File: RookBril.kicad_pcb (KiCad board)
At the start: 2 copper layers, 65 x 55 mm, 69 parts, among them J1 BATT_PINS, J10 TIM3_OUT_CONN, J12 Conn_01x04_Pin, J13 3V_MODE_PINS, J2 IR_SENSOR0_PINS, J3 IR_SENSOR1_PINS, J4 IR_SENSOR2_PINS, J5 IR_SENSOR3_PINS, J6 LOW-BAT_LED_CONN, J7 PDLC_JST_PINS, J9 MCU_MODE_PINS, SW1 SW_Push, U1 VNH7070ASTR, U2 TPS61170DRVR, U3 STM32F411RETx, U4 TPS631000DRLR, Y1 ABM3-8.000MHZ-D2Y-T

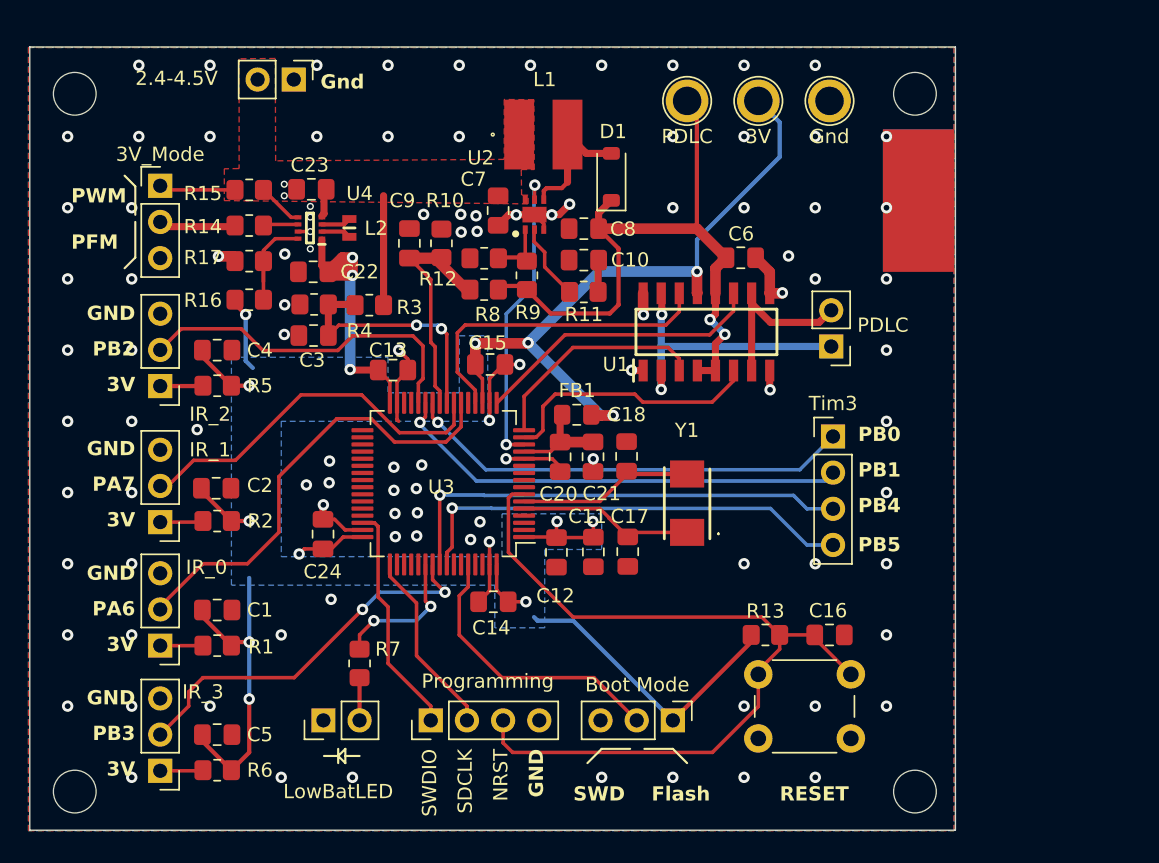
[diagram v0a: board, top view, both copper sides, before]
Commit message: PCBv2.01
Eerste versie van de tweede versie van de pcb prototype.
Nieuwe PDLC voeding, extra pinnen beschikbaar voor GUI inclusief voeding pinnen.
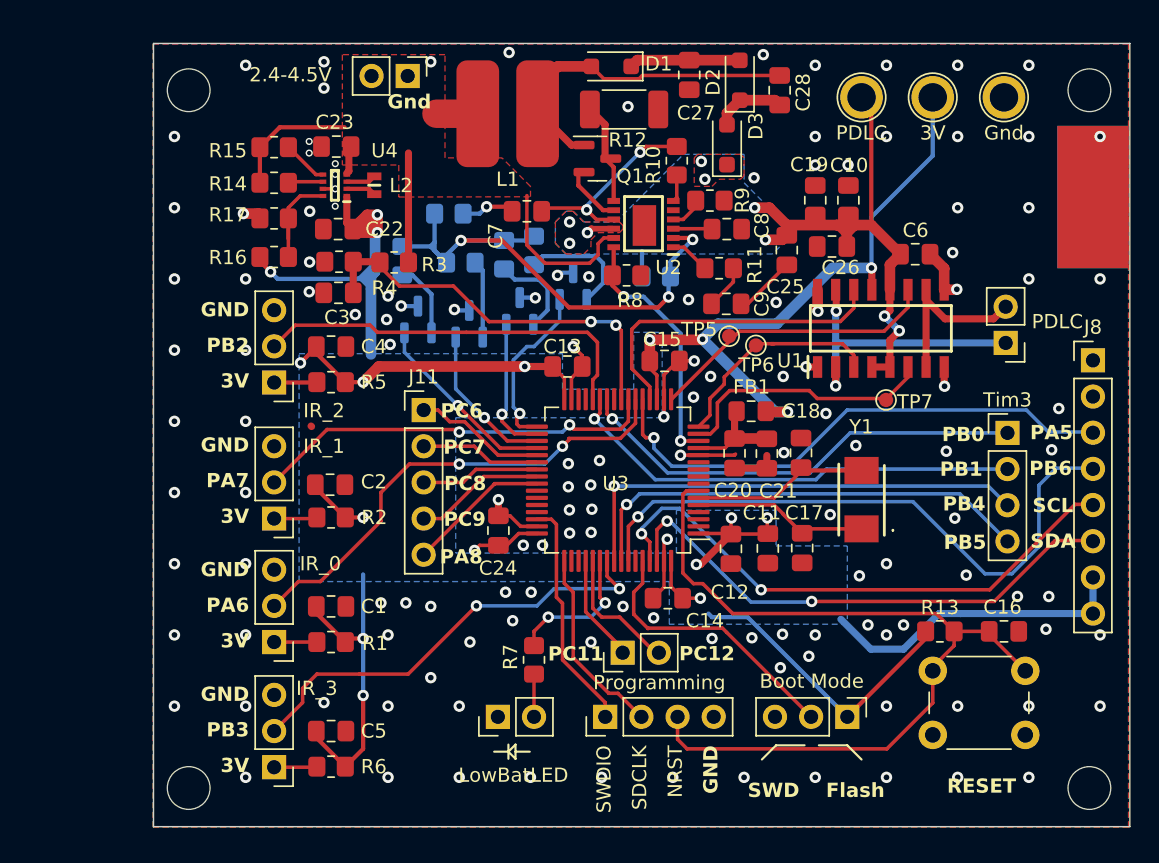
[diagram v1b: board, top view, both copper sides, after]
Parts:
- added C19: 10u, Capacitor_SMD:C_0805_2012Metric_Pad1.18x1.45mm_HandSolder, F.Cu at (170.0, 79.5)
- added C25: 10u, Capacitor_SMD:C_0805_2012Metric_Pad1.18x1.45mm_HandSolder, F.Cu at (168.0, 83.0)
- added C26: 10u, Capacitor_SMD:C_0805_2012Metric_Pad1.18x1.45mm_HandSolder, F.Cu at (171.2, 82.7)
- added C27: 10u, Capacitor_SMD:C_0805_2012Metric_Pad1.18x1.45mm_HandSolder, F.Cu at (161.2, 70.7)
- added C28: 100n, Capacitor_SMD:C_0805_2012Metric_Pad1.18x1.45mm_HandSolder, F.Cu at (167.5, 71.8)
- added D2: ~, Diode_SMD:D_SOD-123F, F.Cu at (164.7, 71.0)
- added D3: ~, Diode_SMD:D_SOD-123F, F.Cu at (163.8, 75.6)
- added J11: Conn_01x05_Pin, Connector_PinHeader_2.54mm:PinHeader_1x05_P2.54mm_Vertical, F.Cu at (142.5, 94.2)
- added J8: Conn_01x08_Pin, Connector_PinHeader_2.54mm:PinHeader_1x08_P2.54mm_Vertical, F.Cu at (189.5, 90.7)
- added Q1: NMOS, Package_TO_SOT_SMD:SOT-23, F.Cu at (154.7, 76.5)
- added Q2: NMOS, Package_TO_SOT_SMD:SOT-23, B.Cu at (142.1, 87.8)
- added Q3: NMOS, Package_TO_SOT_SMD:SOT-23, B.Cu at (145.7, 88.2)
- added Q4: NMOS, Package_TO_SOT_SMD:SOT-23, B.Cu at (149.2, 87.2)
- added Q5: NMOS, Package_TO_SOT_SMD:SOT-23, B.Cu at (153.0, 85.5)
- added R18: 590k, Resistor_SMD:R_0805_2012Metric_Pad1.20x1.40mm_HandSolder, B.Cu at (158.8, 84.8)
- added R19: 47.6k, Resistor_SMD:R_0805_2012Metric_Pad1.20x1.40mm_HandSolder, B.Cu at (144.3, 80.4)
- added R20: 160k, Resistor_SMD:R_0805_2012Metric_Pad1.20x1.40mm_HandSolder, B.Cu at (141.0, 83.7)
- added R21: 80k, Resistor_SMD:R_0805_2012Metric_Pad1.20x1.40mm_HandSolder, B.Cu at (145.1, 83.9)
- added R22: 40k, Resistor_SMD:R_0805_2012Metric_Pad1.20x1.40mm_HandSolder, B.Cu at (148.2, 83.3)
- added R23: 20k, Resistor_SMD:R_0805_2012Metric_Pad1.20x1.40mm_HandSolder, B.Cu at (150.2, 83.0)
- added TP5: TestPoint, TestPoint:TestPoint_Pad_D1.0mm, F.Cu at (163.9, 89.0)
- added TP6: TestPoint, TestPoint:TestPoint_Pad_D1.0mm, F.Cu at (165.8, 89.7)
- added TP7: TestPoint, TestPoint:TestPoint_Pad_D1.0mm, F.Cu at (175.0, 93.5)
- C10: value 680p -> 10u
- C7: value 10u -> 4.7u
- C8: value 10u -> 50n
- C9: value 100n -> 22n
- D1: value MBR0540 -> ~; footprint Diode_SMD:D_SOD-123 -> Diode_SMD:D_SOD-123F
- J13: value 3V_MODE_PINS -> GPIO_OUT_CONN; footprint Connector_PinHeader_2.54mm:PinHeader_1x03_P2.54mm_Vertical -> Connector_PinHeader_2.54mm:PinHeader_1x02_P2.54mm_Vertical
- L1: value VLCF5020T-100M1R1-1 -> 10u; footprint Components:VLCF5020 -> Components:MRS8030T100
- R10: value 10k -> 100k
- R11: value 10k -> 7.5k
- R12: value 39k -> 5m; footprint Resistor_SMD:R_0805_2012Metric_Pad1.20x1.40mm_HandSolder -> Resistor_SMD:R_2010_5025Metric_Pad1.40x2.65mm_HandSolder
- R3: value 50K -> 51k
- R8: value 62k -> 118k
- R9: value 10k -> 41.2k
- U2: value TPS61170DRVR -> ~; footprint Components:SON65P200X200X80-7N -> Components:LT3759
- moved J13 46.1 mm to (156.5, 111.2), turned to 90 degrees
- moved C9 22.7 mm to (163.8, 86.8), turned to 180 degrees
- moved C10 19.0 mm to (172.3, 79.5), turned to -90 degrees
- moved R10 17.5 mm to (160.3, 76.7)
- moved R12 14.3 mm to (156.6, 73.1)
- moved U2 14.0 mm to (163.8, 83.9), turned to 180 degrees
- moved R9 13.9 mm to (162.6, 79.5), turned to 0 degrees
- moved C24 12.3 mm to (147.8, 102.7)
- moved C11 12.3 mm to (166.7, 103.9)
- moved C12 12.3 mm to (164.1, 104.0)
- moved C13 12.3 mm to (152.6, 91.2)
- moved C14 12.3 mm to (159.6, 107.4)
- moved C15 12.3 mm to (159.4, 90.8)
- moved C16 12.3 mm to (183.2, 109.8)
- moved C17 12.3 mm to (169.1, 103.9)
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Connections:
- C10 pad 1: Net-(C10-Pad1) -> GND
- C10 pad 2: GND -> VCC
- C7 pad 1: +BATT -> GND
- C7 pad 2: GND -> Net-(U2-INTVcc)
- C8 pad 1: VCC -> GND
- C8 pad 2: GND -> Net-(U2-SS)
- C9 pad 1: /PDLC-BOOST_VOUT-FB -> GND
- C9 pad 2: GND -> Net-(C9-Pad2)
- D1 pad 1: VCC -> Net-(D1-K)
- J13 pad 1: +BATT -> /MCU/PC11
- J13 pad 2: Net-(J13-Pin_2) -> /MCU/PC12
- R10 pad 1: GND -> Net-(U2-INTVcc)
- R10 pad 2: /PDLC-BOOST_VOUT-FB -> Net-(U2-PGOOD)
- R11 pad 1: Net-(U2-COMP) -> Net-(C9-Pad2)
- R11 pad 2: Net-(C10-Pad1) -> Net-(U2-EN/UVLO)
- R12 pad 1: Net-(U2-FB) -> GND
- R12 pad 2: GND -> Net-(Q1-S)
- R14 pad 1: Net-(J13-Pin_2) -> +BATT
- R8 pad 1: /PDLC-BOOST_VOUT-FB -> /PDLC-BOOST_VOut_EN
- R8 pad 2: VCC -> GND
- R9 pad 1: VCC -> Net-(U2-RT)
- R9 pad 2: Net-(U2-FB) -> GND
- U2 pad 1: Net-(U2-FB) -> Net-(U2-EN/UVLO)
- U2 pad 2: Net-(U2-COMP) -> Net-(U2-FBX)
- U2 pad 3: GND -> Net-(U2-SS)
- U2 pad 4: Net-(D1-A) -> Net-(U2-RT)
- U2 pad 5: /PDLC-BOOST_CTRL -> unconnected-(U2-SYNC-Pad5)
- U2 pad 6: +BATT -> Net-(U2-PGOOD)
- U2 pad 7: GND -> Net-(Q1-S)
- U3 pad 14: /PDLC-BOOST_CTRL -> /PDLC-BOOST_VOut_EN
- U3 pad 25: /PDLC-BOOST_VOUT-FB -> unconnected-(U3-PC5-Pad25)
- U3 pad 33: /MCU/PB12 -> /PDLC-BOOST_VOUT-FBbit3
- U3 pad 34: /MCU/PB13 -> /PDLC-BOOST_VOUT-FBbit2
- U3 pad 35: /MCU/PB14 -> /PDLC-BOOST_VOUT-FBbit1
- U3 pad 36: /MCU/PB15 -> /PDLC-BOOST_VOUT-FBbit0
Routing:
- net +3V0: track 145.6 -> 193.4 mm, vias 16 -> 18
- net /MCU/PB6: track 0.00 -> 43.5 mm, vias 0 -> 1
- net /MCU/PB8: track 0.00 -> 39.7 mm, vias 0 -> 2
- net Net-(U2-FBX): track 0.00 -> 38.0 mm, vias 0 -> 3
- net /MCU/PA5: track 0.00 -> 37.7 mm, vias 0 -> 1
- net /MCU/PB9: track 0.00 -> 37.2 mm, vias 0 -> 2
- net /PDLC-BOOST_CTRL: track 21.4 -> 0.00 mm, vias 2 -> 0
- net +BATT: track 14.3 -> 33.2 mm
- net /PDLC-BOOST_VOUT-FB: track 18.5 -> 0.00 mm
- net /PDLC-BOOST_VOut_EN: track 0.00 -> 17.7 mm, vias 0 -> 2
- net Net-(D1-A): track 9.51 -> 23.5 mm
- net Net-(U2-INTVcc): track 0.00 -> 13.8 mm, vias 0 -> 2
- net /PDLC-BOOST_VOUT-FBbit0: track 0.00 -> 13.5 mm, vias 0 -> 1
- net /PDLC-BOOST_VOUT-FBbit3: track 0.00 -> 12.4 mm, vias 0 -> 1
- net /PDLC-BOOST_VOUT-FBbit1: track 0.00 -> 10.9 mm, vias 0 -> 1
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- added copper zone on B.Cu, net VCC
- added copper zone on F.Cu, net VCC
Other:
- board size 65 x 55 mm -> 68.6 x 55 mm
- board text added: "PA5"
- board text added: "PA8"
- board text added: "PB6"
- board text added: "PC11"
- board text added: "PC12"
- board text added: "PC6"
- board text added: "PC7"
- board text added: "PC8"
- board text added: "PC9"
- board text added: "SCL"
- board text added: "SDA"
- board text removed: "PFM"
- board text removed: "PWM"

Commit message: PCBv2.02
Toepassingen van wouters feedback.
Condensatoren beter geplaatst bij pdlc, mosfet toegevoegd bij fb bat, extra vias toegevoegd en traces verschoven voor betere GND plane connecties
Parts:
- added C29: 4.7u, Capacitor_SMD:C_0805_2012Metric_Pad1.18x1.45mm_HandSolder, F.Cu at (154.5, 90.4)
- added Q6: NMOS, Package_TO_SOT_SMD:SOT-23, B.Cu at (136.3, 87.6)
- added R24: 10k, Resistor_SMD:R_0805_2012Metric_Pad1.20x1.40mm_HandSolder, F.Cu at (139.2, 95.5)
- moved R19 18.8 mm to (162.6, 84.8)
- moved C25 5.03 mm to (167.2, 78.0), turned to 180 degrees
- moved C19 4.78 mm to (167.0, 75.8), turned to 180 degrees
- moved C7 2.10 mm to (151.8, 79.8), turned to -90 degrees
- moved C13 1.67 mm to (150.9, 90.9), turned to 90 degrees
- moved C27 0.53 mm to (161.2, 71.2)
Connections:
- C3 pad 2: GND -> Net-(Q6-D)
- R4 pad 2: GND -> Net-(Q6-D)
- U3 pad 30: unconnected-(U3-VCAP1-Pad30) -> Net-(U3-VCAP1)
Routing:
- net /VBAT_Gate: track 0.00 -> 20.6 mm, vias 0 -> 1
- net GND: track 48.5 -> 56.2 mm, vias 139 -> 159
- net Net-(Q6-D): track 0.00 -> 5.19 mm, vias 0 -> 1
- net VCC: track 39.2 -> 43.2 mm, vias 9 -> 7
- net Net-(U3-VCAP1): track 0.00 -> 3.09 mm
- net Net-(U2-FBX): track 38.0 -> 35.6 mm
- net Net-(D1-A): track 23.5 -> 25.9 mm
- net Net-(D1-K): track 7.81 -> 9.10 mm
- net +BATT: track 33.2 -> 32.1 mm
- net Net-(U2-INTVcc): track 13.8 -> 13.1 mm
- net /VBAT_FB: track 28.0 -> 28.2 mm, vias 2 -> 0
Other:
- board size 68.6 x 55 mm -> 68.6 x 56 mm
- board text added: "3V0"

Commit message: Paar kleine veranderingen, ziet er mooi uit
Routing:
- net +3V0: track 193.2 -> 175.3 mm, vias 18 -> 19
- net GND: track 56.2 -> 43.0 mm, vias 159 -> 158
- net /VBAT_Gate: track 20.6 -> 8.67 mm
- net Net-(J7-Pin_1): track 23.1 -> 19.9 mm
- net Net-(Q4-D): track 6.56 -> 5.12 mm
- net /MCU/PB9: track 37.2 -> 36.2 mm, vias 2 -> 1
- net /H-BRIDGE_PWM: track 20.5 -> 21.5 mm
- net /MCU/PB6: track 43.5 -> 42.9 mm
- net /MCU/PB8: track 39.7 -> 39.1 mm, vias 2 -> 1
